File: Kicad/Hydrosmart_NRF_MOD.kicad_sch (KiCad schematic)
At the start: 9 parts, among them J1 TC2030-IDC-NL, M1 AN54L15Q-U, U2 122, U5 112TR, Y1 FC-135_32.7680KA-AG5

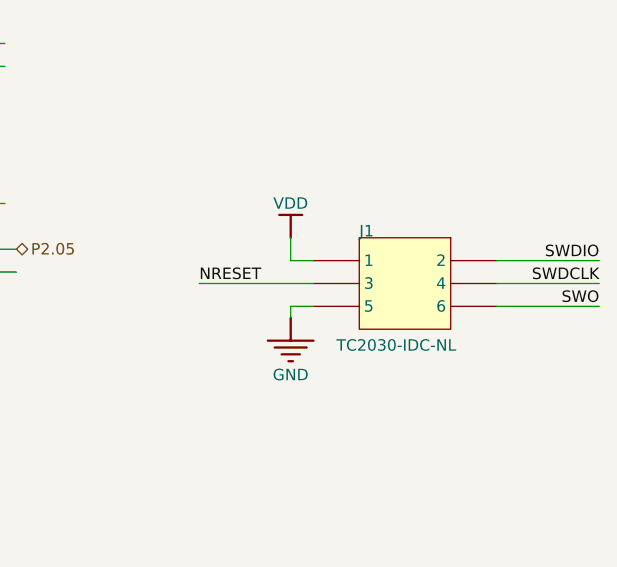
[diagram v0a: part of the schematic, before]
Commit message: + Created library and added information related to BOM: MANUFACTURER and MANUFACTURER PN
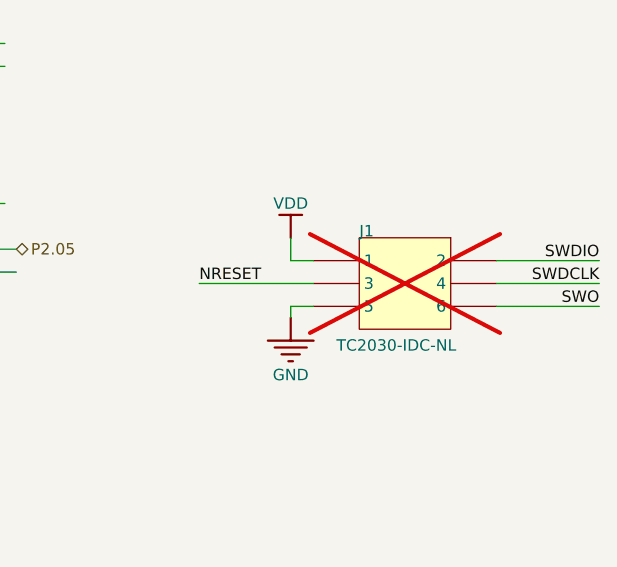
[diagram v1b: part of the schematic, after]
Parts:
- BT1: symbol Hydrosmart_NRF_MOD-altium-import:root_0_Battery_Hydrosmart Revised Schematics_2025-05-28T19_57_34_UTC.SCHLIB -> HydSmart_VA:root_0_Battery_Hydrosmart Revised Schematics_2025-05-28T19_57_34_UTC.SCHLIB; MANUFACTURER (none) -> Jauch Quartz; MANUFACTURER_NAME Jauch Quartz -> (none); MANUFACTURER_PART_NUMBER CR2477 -> (none); MANUFACTURER PN (none) -> CR2477
- C3: value ${CAPACITANCE} -> 4.7uF; symbol Hydrosmart_NRF_MOD-altium-import:root_0_02cd4be3c70576c341d710602a673aa_Altium Content Vault -> HydSmart_VA:root_0_02cd4be3c70576c341d710602a673aa_Altium Content Vault; MANUFACTURER (none) -> Murata Electronics; MANUFACTURER_NAME Murata Electronics -> (none); MANUFACTURER_PART_NUMBER GRM155D81C475ME15J -> (none); MANUFACTURER PN (none) -> GRM155D81C475ME15J
- C4: symbol Hydrosmart_NRF_MOD-altium-import:root_0_02cd4be3c70576c341d710602a673aa_Altium Content Vault -> HydSmart_VA:root_0_02cd4be3c70576c341d710602a673aa_Altium Content Vault; MANUFACTURER (none) -> Murata Electronics; MANUFACTURER_NAME Murata Electronics -> (none); MANUFACTURER_PART_NUMBER GRM155D81C475ME15J -> (none); MANUFACTURER PN (none) -> GRM155D81C475ME15J
- J1: symbol Hydrosmart_NRF_MOD-altium-import:root_0_Header 3X2_Miscellaneous Connectors.IntLib -> HydSmart_VA:root_0_Header 3X2_Miscellaneous Connectors.IntLib; now not fitted
- L2: symbol Hydrosmart_NRF_MOD-altium-import:root_3_mirrored_725321dda6339637d4d059423bc1c3c_Altium Content Vault -> HydSmart_VA:root_3_mirrored_725321dda6339637d4d059423bc1c3c_Altium Content Vault; MANUFACTURER (none) -> TDK Corporation; MANUFACTURER_NAME TDK Corporation -> (none); MANUFACTURER_PART_NUMBER MLZ1608E4R7MT000 -> (none); MANUFACTURER PN (none) -> MLZ1608E4R7MT000
- M1: symbol Hydrosmart_NRF_MOD-altium-import:root_0_AN54L15Q-U_Ubihere -> HydSmart_VA:root_0_AN54L15Q-U_Ubihere; MANUFACTURER (none) -> Raytac; MANUFACTURER_NAME Raytac -> (none); MANUFACTURER_PART_NUMBER AN54L15Q-U -> (none); MANUFACTURER PN (none) -> AN54L15Q-U
- U2: symbol Hydrosmart_NRF_MOD-altium-import:root_2_TEST_POINT_DARTMX8M_Carrier.SchLib -> HydSmart_VA:root_2_TEST_POINT_DARTMX8M_Carrier.SchLib; MANUFACTURER (none) -> Keystone Electronics; MANUFACTURER_NAME Keystone Electronics -> (none); MANUFACTURER_PART_NUMBER 122 -> (none); MANUFACTURER PN (none) -> 122
- U5: symbol Hydrosmart_NRF_MOD-altium-import:root_0_TEST_POINT_DARTMX8M_Carrier.SchLib -> HydSmart_VA:root_0_TEST_POINT_DARTMX8M_Carrier.SchLib; MANUFACTURER (none) -> Keystone Electronics; MANUFACTURER_NAME Keystone Electronics -> (none); MANUFACTURER_PART_NUMBER 112TR -> (none); MANUFACTURER PN (none) -> 112TR
- Y1: symbol Hydrosmart_NRF_MOD-altium-import:root_1_FC-135_32.7680KA-AG5_Ubihere -> HydSmart_VA:root_1_FC-135_32.7680KA-AG5_Ubihere; MANUFACTURER (none) -> Epson Timing; MANUFACTURER_NAME Epson Timing -> (none); MANUFACTURER_PART_NUMBER FC-135 32.7680KA-AG5 -> (none); MANUFACTURER PN (none) -> FC-135 32.7680KA-AG5
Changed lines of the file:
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@@
 	)
 	(symbol
-		(lib_id "Hydrosmart_NRF_MOD-altium-import:root_0_TEST_POINT_DARTMX8M_Carrier.SchLib")
+		(lib_id "HydSmart_VA:root_0_TEST_POINT_DARTMX8M_Carrier.SchLib")
 		(at 130.81 165.1 0)
 		(unit 1)
@@
 			)
 		)
-		(property "MANUFACTURER_NAME" "Keystone Electronics"
-			(at 127.762 161.544 0)
-			(effects
-				(font
-					(size 1.27 1.27)
-				)
-				(justify left bottom)
-				(hide yes)
-			)
-		)
-		(property "MANUFACTURER_PART_NUMBER" "112TR"
-			(at 127.762 161.544 0)
-			(effects
-				(font
-					(size 1.27 1.27)
-				)
-				(justify left bottom)
+		(property "MANUFACTURER" "Keystone Electronics"
+			(at 130.81 165.1 0)
+			(effects
+				(font
+					(size 1.27 1.27)
+				)
+				(hide yes)
+			)
+		)
+		(property "MANUFACTURER PN" "112TR"
+			(at 130.81 165.1 0)
+			(effects
+				(font
+					(size 1.27 1.27)
+				)
 				(hide yes)
 			)
@@
 	)
 	(symbol
-		(lib_id "Hydrosmart_NRF_MOD-altium-import:root_0_02cd4be3c70576c341d710602a673aa_Altium Content Vault")
+		(lib_id "HydSmart_VA:root_0_02cd4be3c70576c341d710602a673aa_Altium Content Vault")
 		(at 176.53 97.79 0)
 		(unit 1)
@@
 			)
 		)
-		(property "MANUFACTURER_NAME" "Murata Electronics"
-			(at 173.736 97.282 0)
-			(effects
-				(font
-					(size 1.27 1.27)
-				)
-				(justify left bottom)
-				(hide yes)
-			)
-		)
-		(property "MANUFACTURER_PART_NUMBER" "GRM155D81C475ME15J"
-			(at 173.736 97.282 0)
-			(effects
-				(font
-					(size 1.27 1.27)
-				)
-				(justify left bottom)
+		(property "MANUFACTURER" "Murata Electronics"
+			(at 176.53 97.79 0)
+			(effects
+				(font
+					(size 1.27 1.27)
+				)
+				(hide yes)
+			)
+		)
+		(property "MANUFACTURER PN" "GRM155D81C475ME15J"
+			(at 176.53 97.79 0)
+			(effects
+				(font
+					(size 1.27 1.27)
+				)
 				(hide yes)
 			)
@@
 	)
 	(symbol
-		(lib_id "Hydrosmart_NRF_MOD-altium-import:root_0_AN54L15Q-U_Ubihere")
+		(lib_id "HydSmart_VA:root_0_AN54L15Q-U_Ubihere")
 		(at 148.59 73.66 0)
 		(unit 1)
@@
 			)
 		)
-		(property "MANUFACTURER_NAME" "Raytac"
-			(at 122.682 43.18 0)
-			(effects
-				(font
-					(size 1.27 1.27)
-				)
-				(justify left bottom)
-				(hide yes)
-			)
-		)
-		(property "MANUFACTURER_PART_NUMBER" "AN54L15Q-U"
-			(at 122.682 43.18 0)
-			(effects
-				(font
-					(size 1.27 1.27)
-				)
-				(justify left bottom)
+		(property "MANUFACTURER" "Raytac"
+			(at 148.59 73.66 0)
+			(effects
+				(font
+					(size 1.27 1.27)
+				)
+				(hide yes)
+			)
+		)
+		(property "MANUFACTURER PN" "AN54L15Q-U"
+			(at 148.59 73.66 0)
+			(effects
+				(font
+					(size 1.27 1.27)
+				)
 				(hide yes)
 			)
@@
 	)
 	(symbol
-		(lib_id "Hydrosmart_NRF_MOD-altium-import:root_0_Header 3X2_Miscellaneous Connectors.IntLib")
+		(lib_id "HydSmart_VA:root_0_Header 3X2_Miscellaneous Connectors.IntLib")
 		(at 234.95 85.09 0)
 		(unit 1)
@@
 		(in_bom yes)
 		(on_board yes)
-		(dnp no)
+		(dnp yes)
 		(property "Reference" "J1"
 			(at 234.95 85.09 0)
@@
 	)
 	(symbol
-		(lib_id "Hydrosmart_NRF_MOD-altium-import:root_3_mirrored_725321dda6339637d4d059423bc1c3c_Altium Content Vault")
+		(lib_id "HydSmart_VA:root_3_mirrored_725321dda6339637d4d059423bc1c3c_Altium Content Vault")
 		(at 91.44 66.04 0)
 		(unit 1)
@@
 			)
 		)
-		(property "MANUFACTURER_NAME" "TDK Corporation"
-			(at 90.17 65.532 0)
-			(effects
-				(font
-					(size 1.27 1.27)
-				)
-				(justify left bottom)
-				(hide yes)
-			)
-		)
-		(property "MANUFACTURER_PART_NUMBER" "MLZ1608E4R7MT000"
-			(at 90.17 65.532 0)
-			(effects
-				(font
-					(size 1.27 1.27)
-				)
-				(justify left bottom)
+		(property "MANUFACTURER" "TDK Corporation"
+			(at 91.44 66.04 0)
+			(effects
+				(font
+					(size 1.27 1.27)
+				)
+				(hide yes)
+			)
+		)
+		(property "MANUFACTURER PN" "MLZ1608E4R7MT000"
+			(at 91.44 66.04 0)
+			(effects
+				(font
+					(size 1.27 1.27)
+				)
 				(hide yes)
 			)
@@
 	)
 	(symbol
-		(lib_id "Hydrosmart_NRF_MOD-altium-import:root_1_FC-135_32.7680KA-AG5_Ubihere")
+		(lib_id "HydSmart_VA:root_1_FC-135_32.7680KA-AG5_Ubihere")
 		(at 91.44 106.68 0)
 		(unit 1)
@@
 			)
 		)
-		(property "MANUFACTURER_PART_NUMBER" "FC-135 32.7680KA-AG5"
-			(at 87.884 96.012 0)
-			(effects
-				(font
-					(size 1.27 1.27)
-				)
-				(justify left bottom)
-				(hide yes)
-			)
-		)
 		(property "HEIGHT" "0.9mm"
 			(at 87.884 96.012 0)
@@
 			)
 		)
-		(property "MANUFACTURER_NAME" "Epson Timing"
-			(at 87.884 96.012 0)
-			(effects
-				(font
-					(size 1.27 1.27)
-				)
-				(justify left bottom)
-				(hide yes)
-			)
-		)
 		(property "ARROW PART NUMBER" "FC-135 32.7680KA-AG5"
 			(at 87.884 96.012 0)
@@
 				)
 				(justify left bottom)
+				(hide yes)
+			)
+		)
+		(property "MANUFACTURER" "Epson Timing"
+			(at 91.44 106.68 0)
+			(effects
+				(font
+					(size 1.27 1.27)
+				)
+				(hide yes)
+			)
+		)
+		(property "MANUFACTURER PN" "FC-135 32.7680KA-AG5"
+			(at 91.44 106.68 0)
+			(effects
+				(font
+					(size 1.27 1.27)
+				)
 				(hide yes)
 			)
@@
 	)
 	(symbol
-		(lib_id "Hydrosmart_NRF_MOD-altium-import:root_2_TEST_POINT_DARTMX8M_Carrier.SchLib")
+		(lib_id "HydSmart_VA:root_2_TEST_POINT_DARTMX8M_Carrier.SchLib")
 		(at 110.49 160.02 0)
 		(unit 1)
@@
 			)
 		)
-		(property "MANUFACTURER_NAME" "Keystone Electronics"
-			(at 104.14 161.29 0)
-			(effects
-				(font
-					(size 1.27 1.27)
-				)
-				(justify left bottom)
-				(hide yes)
-			)
-		)
-		(property "MANUFACTURER_PART_NUMBER" "122"
-			(at 104.14 161.29 0)
-			(effects
-				(font
-					(size 1.27 1.27)
-				)
-				(justify left bottom)
+		(property "MANUFACTURER" "Keystone Electronics"
+			(at 110.49 160.02 0)
+			(effects
+				(font
+					(size 1.27 1.27)
+				)
+				(hide yes)
+			)
+		)
+		(property "MANUFACTURER PN" "122"
+			(at 110.49 160.02 0)
+			(effects
+				(font
+					(size 1.27 1.27)
+				)
 				(hide yes)
 			)
@@
 	)
 	(symbol
-		(lib_id "Hydrosmart_NRF_MOD-altium-import:root_0_Battery_Hydrosmart Revised Schematics_2025-05-28T19_57_34_UTC.SCHLIB")
+		(lib_id "HydSmart_VA:root_0_Battery_Hydrosmart Revised Schematics_2025-05-28T19_57_34_UTC.SCHLIB")
 		(at 148.59 162.56 0)
 		(unit 1)
@@
 			)
 		)
-		(property "MANUFACTURER_NAME" "Jauch Quartz"
-			(at 145.288 160.02 0)
-			(effects
-				(font
-					(size 1.27 1.27)
-				)
-				(justify left bottom)
-				(hide yes)
-			)
-		)
-		(property "MANUFACTURER_PART_NUMBER" "CR2477"
-			(at 145.288 160.02 0)
-			(effects
-				(font
-					(size 1.27 1.27)
-				)
-				(justify left bottom)
+		(property "MANUFACTURER" "Jauch Quartz"
+			(at 148.59 162.56 0)
+			(effects
+				(font
+					(size 1.27 1.27)
+				)
+				(hide yes)
+			)
+		)
+		(property "MANUFACTURER PN" "CR2477"
+			(at 148.59 162.56 0)
+			(effects
+				(font
+					(size 1.27 1.27)
+				)
 				(hide yes)
 			)
@@
 	)
 	(symbol
-		(lib_id "Hydrosmart_NRF_MOD-altium-import:root_0_02cd4be3c70576c341d710602a673aa_Altium Content Vault")
+		(lib_id "HydSmart_VA:root_0_02cd4be3c70576c341d710602a673aa_Altium Content Vault")
 		(at 100.33 81.28 0)
 		(unit 1)
@@
 			)
 		)
-		(property "Value" "${CAPACITANCE}"
+		(property "Value" "4.7uF"
 			(at 103.124 87.122 0)
 			(effects
@@
 			)
 		)
-		(property "MANUFACTURER_NAME" "Murata Electronics"
-			(at 97.536 80.772 0)
-			(effects
-				(font
-					(size 1.27 1.27)
-				)
-				(justify left bottom)
-				(hide yes)
-			)
-		)
-		(property "MANUFACTURER_PART_NUMBER" "GRM155D81C475ME15J"
-			(at 97.536 80.772 0)
-			(effects
-				(font
-					(size 1.27 1.27)
-				)
-				(justify left bottom)
-				(hide yes)
-			)
+		(property "MANUFACTURER" "Murata Electronics"
+			(at 100.33 81.28 0)
+			(effects
+				(font
+					(size 1.27 1.27)
+				)
+				(hide yes)
+			)
+		)
+		(property "MANUFACTURER PN" "GRM155D81C475ME15J"
+			(at 100.33 81.28 0)
+			(effects
+				(font
+					(size 1.27 1.27)
+				)
+				(hide yes)
+			)
